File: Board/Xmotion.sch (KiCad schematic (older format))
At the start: 41 parts, among them J1 DB25, J2 DB25

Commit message: Board is layed out
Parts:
- added K1: FAN1, connect:SIL-3, symbol CONN_3
- added K4: FAN4, connect:SIL-3, symbol CONN_3
- added P100, P200, P300, P400: CONN_1, symbol CONN_1
- J1, J2: footprint (none) -> connect:DB25MC
- K2: renamed from K?; value FAN1 -> FAN2; footprint (none) -> connect:SIL-3
- K3: renamed from K?; value FAN2 -> FAN3; footprint (none) -> connect:SIL-3
- P1, P10, P11, P12, P13, P14, P15, P16, P17, P18, P19, P2, P20, P21, P22, P23, P24, P25, P3, P4, P5, P6, P7, P8, P9: renamed from P?; footprint (none) -> Xmotion:PLUGABLE_HEADER
- Q1, Q2, Q3, Q4, Q5, Q6: renamed from Q?; footprint TO220 -> Xmotion:TO220
- R1, R2, R3, R4, R5, R6: renamed from R?; footprint (none) -> discret:R3
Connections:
- wire segments 209 -> 213
- no-connect marks 7 -> 12

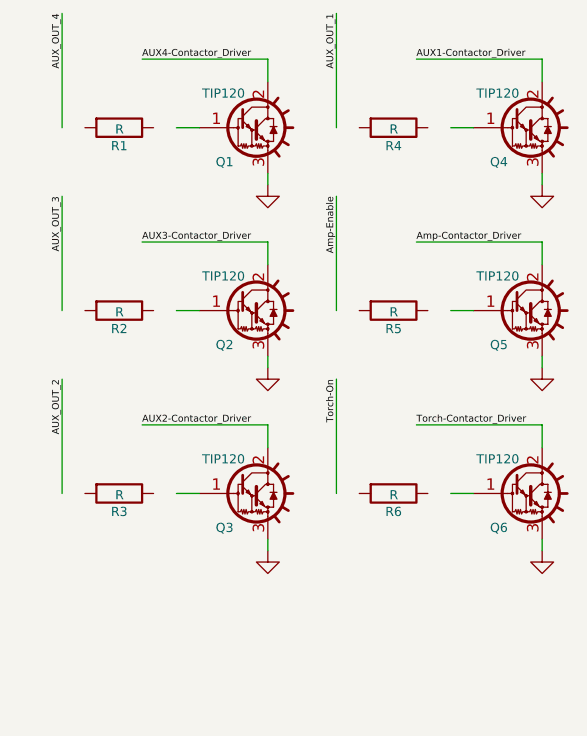
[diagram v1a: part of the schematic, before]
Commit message: Board is routed
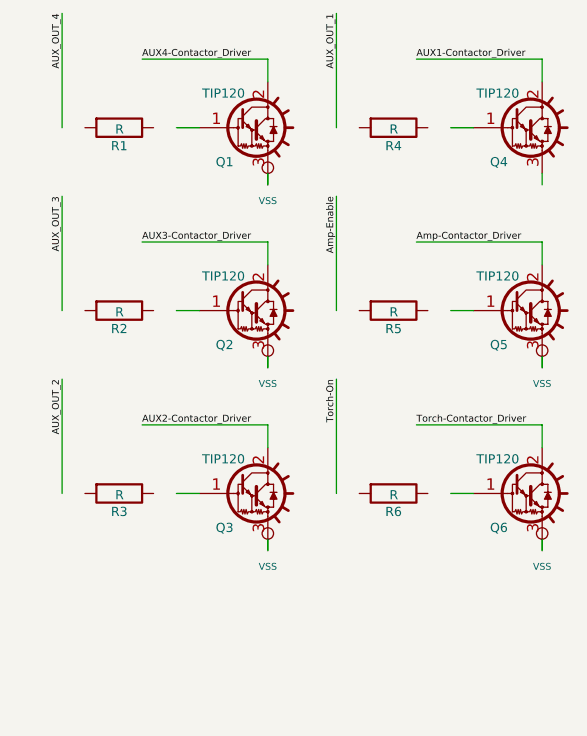
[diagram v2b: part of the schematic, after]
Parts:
- P100, P200, P300, P400: footprint (none) -> Xmotion:BOLT_HOLE
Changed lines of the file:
@@
-$EndComp
-$Comp
-L GND #PWR082
-U 1 1 59A7D273
-P 2300 5600
-F 0 "#PWR082" H 2300 5600 30  0001 C CNN
-F 1 "GND" H 2300 5530 30  0001 C CNN
-F 2 "" H 2300 5600 60  0001 C CNN
-F 3 "" H 2300 5600 60  0001 C CNN
-	1    2300 5600
-	-1   0    0    1
 $EndComp
 $Comp
@@
 	10800 5800 10800 5900
 $Comp
-L GND #PWR085
-U 1 1 59A7FBBE
-P 10800 6350
-F 0 "#PWR085" H 10800 6350 30  0001 C CNN
-F 1 "GND" H 10800 6280 30  0001 C CNN
-F 2 "" H 10800 6350 60  0001 C CNN
-F 3 "" H 10800 6350 60  0001 C CNN
-	1    10800 6350
-	1    0    0    -1
-$EndComp
-$Comp
 L R R6
 U 1 1 59A7FC06
@@
 	10800 5000 10800 5100
 $Comp
-L GND #PWR086
-U 1 1 59A80D25
-P 10800 5550
-F 0 "#PWR086" H 10800 5550 30  0001 C CNN
-F 1 "GND" H 10800 5480 30  0001 C CNN
-F 2 "" H 10800 5550 60  0001 C CNN
-F 3 "" H 10800 5550 60  0001 C CNN
-	1    10800 5550
-	1    0    0    -1
-$EndComp
-$Comp
 L R R5
 U 1 1 59A80D2B
@@
 Wire Wire Line
 	10800 4200 10800 4300
-$Comp
-L GND #PWR087
-U 1 1 59A81DC0
-P 10800 4750
-F 0 "#PWR087" H 10800 4750 30  0001 C CNN
-F 1 "GND" H 10800 4680 30  0001 C CNN
-F 2 "" H 10800 4750 60  0001 C CNN
-F 3 "" H 10800 4750 60  0001 C CNN
-	1    10800 4750
-	1    0    0    -1
-$EndComp
 $Comp
 L R R4
@@
 	9600 5800 9600 5900
 $Comp
-L GND #PWR088
-U 1 1 59A82CF5
-P 9600 6350
-F 0 "#PWR088" H 9600 6350 30  0001 C CNN
-F 1 "GND" H 9600 6280 30  0001 C CNN
-F 2 "" H 9600 6350 60  0001 C CNN
-F 3 "" H 9600 6350 60  0001 C CNN
-	1    9600 6350
-	1    0    0    -1
-$EndComp
-$Comp
 L R R3
 U 1 1 59A82CFB
@@
 	9600 5000 9600 5100
 $Comp
-L GND #PWR089
-U 1 1 59A83002
-P 9600 5550
-F 0 "#PWR089" H 9600 5550 30  0001 C CNN
-F 1 "GND" H 9600 5480 30  0001 C CNN
-F 2 "" H 9600 5550 60  0001 C CNN
-F 3 "" H 9600 5550 60  0001 C CNN
-	1    9600 5550
-	1    0    0    -1
-$EndComp
-$Comp
 L R R2
 U 1 1 59A83008
@@
 Wire Wire Line
 	9600 4200 9600 4300
-$Comp
-L GND #PWR090
-U 1 1 59A8377D
-P 9600 4750
-F 0 "#PWR090" H 9600 4750 30  0001 C CNN
-F 1 "GND" H 9600 4680 30  0001 C CNN
-F 2 "" H 9600 4750 60  0001 C CNN
-F 3 "" H 9600 4750 60  0001 C CNN
-	1    9600 4750
-	1    0    0    -1
-$EndComp
 $Comp
 L R R1
@@
 	1300 3900 1650 3900
 $Comp
-L GND #PWR091
+L GND #PWR085
 U 1 1 59A85377
 P 1650 4300
-F 0 "#PWR091" H 1650 4300 30  0001 C CNN
+F 0 "#PWR085" H 1650 4300 30  0001 C CNN
 F 1 "GND" H 1650 4230 30  0001 C CNN
 F 2 "" H 1650 4300 60  0001 C CNN
@@
 $EndComp
 $Comp
-L GND #PWR092
+L GND #PWR086
 U 1 1 59A8537D
 P 1650 4200
-F 0 "#PWR092" H 1650 4200 30  0001 C CNN
+F 0 "#PWR086" H 1650 4200 30  0001 C CNN
 F 1 "GND" H 1650 4130 30  0001 C CNN
 F 2 "" H 1650 4200 60  0001 C CNN
@@
 $EndComp
 $Comp
-L GND #PWR093
+L GND #PWR087
 U 1 1 59A85383
 P 1650 4100
-F 0 "#PWR093" H 1650 4100 30  0001 C CNN
+F 0 "#PWR087" H 1650 4100 30  0001 C CNN
 F 1 "GND" H 1650 4030 30  0001 C CNN
 F 2 "" H 1650 4100 60  0001 C CNN
@@
 $EndComp
 $Comp
-L GND #PWR094
+L GND #PWR088
 U 1 1 59A85389
 P 1650 4000
-F 0 "#PWR094" H 1650 4000 30  0001 C CNN
+F 0 "#PWR088" H 1650 4000 30  0001 C CNN
 F 1 "GND" H 1650 3930 30  0001 C CNN
 F 2 "" H 1650 4000 60  0001 C CNN
@@
 	1300 2800 1650 2800
 $Comp
-L GND #PWR095
+L GND #PWR089
 U 1 1 59A8538F
 P 1650 3900
-F 0 "#PWR095" H 1650 3900 30  0001 C CNN
+F 0 "#PWR089" H 1650 3900 30  0001 C CNN
 F 1 "GND" H 1650 3830 30  0001 C CNN
 F 2 "" H 1650 3900 60  0001 C CNN
@@
 $EndComp
 $Comp
-L VDD #PWR096
+L VDD #PWR090
 U 1 1 59A85CDF
 P 1650 3750
-F 0 "#PWR096" H 1650 3850 30  0001 C CNN
+F 0 "#PWR090" H 1650 3850 30  0001 C CNN
 F 1 "VDD" H 1650 3860 30  0000 C CNN
 F 2 "" H 1650 3750 60  0001 C CNN
@@
 $EndComp
 $Comp
-L VDD #PWR097
+L VDD #PWR091
 U 1 1 59A8618F
 P 1650 3650
-F 0 "#PWR097" H 1650 3750 30  0001 C CNN
+F 0 "#PWR091" H 1650 3750 30  0001 C CNN
 F 1 "VDD" H 1650 3760 30  0000 C CNN
 F 2 "" H 1650 3650 60  0001 C CNN
@@
 $EndComp
 $Comp
-L VDD #PWR098
+L VDD #PWR092
 U 1 1 59A8623E
 P 1650 3550
-F 0 "#PWR098" H 1650 3650 30  0001 C CNN
+F 0 "#PWR092" H 1650 3650 30  0001 C CNN
 F 1 "VDD" H 1650 3660 30  0000 C CNN
 F 2 "" H 1650 3550 60  0001 C CNN
@@
 $EndComp
 $Comp
-L VDD #PWR099
+L VDD #PWR093
 U 1 1 59A862C4
 P 1650 3450
-F 0 "#PWR099" H 1650 3550 30  0001 C CNN
+F 0 "#PWR093" H 1650 3550 30  0001 C CNN
 F 1 "VDD" H 1650 3560 30  0000 C CNN
 F 2 "" H 1650 3450 60  0001 C CNN
@@
 $EndComp
 $Comp
-L VDD #PWR0100
+L VDD #PWR094
 U 1 1 59A8634A
 P 1650 3350
-F 0 "#PWR0100" H 1650 3450 30  0001 C CNN
+F 0 "#PWR094" H 1650 3450 30  0001 C CNN
 F 1 "VDD" H 1650 3460 30  0000 C CNN
 F 2 "" H 1650 3350 60  0001 C CNN
@@
 $EndComp
 $Comp
-L +12V #PWR0101
+L +12V #PWR095
 U 1 1 59A865E5
 P 1650 3200
-F 0 "#PWR0101" H 1650 3150 20  0001 C CNN
+F 0 "#PWR095" H 1650 3150 20  0001 C CNN
 F 1 "+12V" H 1650 3300 30  0000 C CNN
 F 2 "" H 1650 3200 60  0001 C CNN
@@
 $EndComp
 $Comp
-L +12V #PWR0102
+L +12V #PWR096
 U 1 1 59A8694D
 P 1650 3100
-F 0 "#PWR0102" H 1650 3050 20  0001 C CNN
+F 0 "#PWR096" H 1650 3050 20  0001 C CNN
 F 1 "+12V" H 1650 3200 30  0000 C CNN
 F 2 "" H 1650 3100 60  0001 C CNN
@@
 $EndComp
 $Comp
-L +12V #PWR0103
+L +12V #PWR097
 U 1 1 59A869D3
 P 1650 3000
-F 0 "#PWR0103" H 1650 2950 20  0001 C CNN
+F 0 "#PWR097" H 1650 2950 20  0001 C CNN
 F 1 "+12V" H 1650 3100 30  0000 C CNN
 F 2 "" H 1650 3000 60  0001 C CNN
@@
 $EndComp
 $Comp
-L +12V #PWR0104
+L +12V #PWR098
 U 1 1 59A86A59
 P 1650 2900
-F 0 "#PWR0104" H 1650 2850 20  0001 C CNN
+F 0 "#PWR098" H 1650 2850 20  0001 C CNN
 F 1 "+12V" H 1650 3000 30  0000 C CNN
 F 2 "" H 1650 2900 60  0001 C CNN
@@
 $EndComp
 $Comp
-L +12V #PWR0105
+L +12V #PWR099
 U 1 1 59A86B08
 P 1650 2800
-F 0 "#PWR0105" H 1650 2750 20  0001 C CNN
+F 0 "#PWR099" H 1650 2750 20  0001 C CNN
 F 1 "+12V" H 1650 2900 30  0000 C CNN
 F 2 "" H 1650 2800 60  0001 C CNN
@@
 	9250 2650 9250 2400
 $Comp
-L GND #PWR0106
+L GND #PWR0100
 U 1 1 59A8789B
 P 9250 2400
-F 0 "#PWR0106" H 9250 2400 30  0001 C CNN
+F 0 "#PWR0100" H 9250 2400 30  0001 C CNN
 F 1 "GND" H 9250 2330 30  0001 C CNN
 F 2 "" H 9250 2400 60  0001 C CNN
@@
 $EndComp
 $Comp
-L +12V #PWR0107
+L +12V #PWR0101
 U 1 1 59A878A1
 P 9150 2400
-F 0 "#PWR0107" H 9150 2350 20  0001 C CNN
+F 0 "#PWR0101" H 9150 2350 20  0001 C CNN
 F 1 "+12V" H 9150 2500 30  0000 C CNN
 F 2 "" H 9150 2400 60  0001 C CNN
@@
 	10500 2650 10500 2400
 $Comp
-L GND #PWR0108
+L GND #PWR0102
 U 1 1 59A87976
 P 10500 2400
-F 0 "#PWR0108" H 10500 2400 30  0001 C CNN
+F 0 "#PWR0102" H 10500 2400 30  0001 C CNN
 F 1 "GND" H 10500 2330 30  0001 C CNN
 F 2 "" H 10500 2400 60  0001 C CNN
@@
 $EndComp
 $Comp
-L +12V #PWR0109
+L +12V #PWR0103
 U 1 1 59A8797C
 P 10400 2400
-F 0 "#PWR0109" H 10400 2350 20  0001 C CNN
+F 0 "#PWR0103" H 10400 2350 20  0001 C CNN
 F 1 "+12V" H 10400 2500 30  0000 C CNN
 F 2 "" H 10400 2400 60  0001 C CNN
@@
 F 0 "P100" H 3730 3250 40  0000 L CNN
 F 1 "CONN_1" H 3650 3305 30  0001 C CNN
-F 2 "" H 3650 3250 60  0000 C CNN
+F 2 "Xmotion:BOLT_HOLE" H 3650 3250 60  0001 C CNN
 F 3 "" H 3650 3250 60  0000 C CNN
 	1    3650 3250
@@
 F 0 "P200" H 3730 3400 40  0000 L CNN
 F 1 "CONN_1" H 3650 3455 30  0001 C CNN
-F 2 "" H 3650 3400 60  0000 C CNN
+F 2 "Xmotion:BOLT_HOLE" H 3650 3400 60  0001 C CNN
 F 3 "" H 3650 3400 60  0000 C CNN
 	1    3650 3400
@@
 F 0 "P300" H 3730 3550 40  0000 L CNN
 F 1 "CONN_1" H 3650 3605 30  0001 C CNN
-F 2 "" H 3650 3550 60  0000 C CNN
+F 2 "Xmotion:BOLT_HOLE" H 3650 3550 60  0001 C CNN
 F 3 "" H 3650 3550 60  0000 C CNN
 	1    3650 3550
@@
 F 0 "P400" H 3730 3700 40  0000 L CNN
 F 1 "CONN_1" H 3650 3755 30  0001 C CNN
-F 2 "" H 3650 3700 60  0000 C CNN
+F 2 "Xmotion:BOLT_HOLE" H 3650 3700 60  0001 C CNN
 F 3 "" H 3650 3700 60  0000 C CNN
 	1    3650 3700
@@
 NoConn ~ 3500 3550
 NoConn ~ 3500 3700
+$Comp
+L VSS #PWR0104
+U 1 1 59A90645
+P 9600 6350
+F 0 "#PWR0104" H 9600 6350 30  0001 C CNN
+F 1 "VSS" H 9600 6280 30  0000 C CNN
+F 2 "" H 9600 6350 60  0001 C CNN
+F 3 "" H 9600 6350 60  0001 C CNN
+	1    9600 6350
+	1    0    0    -1
+$EndComp
+$Comp
+L VSS #PWR0105
+U 1 1 59A90940
+P 10800 6350
+F 0 "#PWR0105" H 10800 6350 30  0001 C CNN
+F 1 "VSS" H 10800 6280 30  0000 C CNN
+F 2 "" H 10800 6350 60  0001 C CNN
+F 3 "" H 10800 6350 60  0001 C CNN
+	1    10800 6350
+	1    0    0    -1
+$EndComp
+$Comp
+L VSS #PWR0106
+U 1 1 59A90A65
+P 9600 5550
+F 0 "#PWR0106" H 9600 5550 30  0001 C CNN
+F 1 "VSS" H 9600 5480 30  0000 C CNN
+F 2 "" H 9600 5550 60  0001 C CNN
+F 3 "" H 9600 5550 60  0001 C CNN
+	1    9600 5550
+	1    0    0    -1
+$EndComp
+$Comp
+L VSS #PWR0107
+U 1 1 59A90AFD
+P 10800 5550
+F 0 "#PWR0107" H 10800 5550 30  0001 C CNN
+F 1 "VSS" H 10800 5480 30  0000 C CNN
+F 2 "" H 10800 5550 60  0001 C CNN
+F 3 "" H 10800 5550 60  0001 C CNN
+	1    10800 5550
+	1    0    0    -1
+$EndComp
+$Comp
+L VSS #PWR0108
+U 1 1 59A90BC4
+P 9600 4750
+F 0 "#PWR0108" H 9600 4750 30  0001 C CNN
+F 1 "VSS" H 9600 4680 30  0000 C CNN
+F 2 "" H 9600 4750 60  0001 C CNN
+F 3 "" H 9600 4750 60  0001 C CNN
+	1    9600 4750
+	1    0    0    -1
+$EndComp
+$Comp
+L GND #PWR082
+U 1 1 59A7D273
+P 2300 5600
+F 0 "#PWR082" H 2300 5600 30  0001 C CNN
+F 1 "GND" H 2300 5530 30  0001 C CNN
+F 2 "" H 2300 5600 60  0001 C CNN
+F 3 "" H 2300 5600 60  0001 C CNN
+	1    2300 5600
+	-1   0    0    1
+$EndComp
 $EndSCHEMATC

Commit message: Updated Schematic, fixed pinmap to work with Mesa 5i25 G540 Firmware and added opto-isolators
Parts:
- removed P100, P200, P300, P400: CONN_1, Xmotion:BOLT_HOLE, symbol CONN_1
- removed Q2, Q3, Q4, Q5, Q6: TIP120, Xmotion:TO220, symbol TIP120
- removed R2, R3, R4, R5, R6: R, discret:R3, symbol R
- added Q? (x5): TIP120, Xmotion:TO220, symbol TIP120
- added R? (x6): 220, symbol R
- added R? (x5): 1K, discret:R3, symbol R
- added U? (x6): 4N25, DIP-6, symbol 4N25
- K1, K2, K3, K4: symbol CONN_3 -> CONN_01X03
- P1, P10, P11, P12, P13, P14, P15, P16, P17, P18, P19, P2, P20, P21, P22, P23, P24, P25, P3, P4, P5, P6, P7, P8, P9: symbol CONN_5 -> CONN_01X05
- R1: value R -> 1K
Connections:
- net labels added: Y1-Home, Y2-Home
- wire segments 213 -> 261
- no-connect marks 12 -> 13
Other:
- moved on the sheet: K1, K2, K3, K4, Q1, R1

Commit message: Board is ready to be routed
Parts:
- J1, J2: footprint connect:DB25MC -> Xmotion:DB25MC
- U1, U2, U3, U4, U5, U6: renamed from U?; footprint DIP-6 -> Housings_DIP:DIP-6_W7.62mm
- gave numbers to parts that had none: 16
- renumbered R1 to R7
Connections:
- net Y-Home is gone; now on net Y1-Home: P15.2 (P2)
- net GND: no longer P10.1 (P1), P14.1 (P1), P19.1 (P1), P6.1 (P1), R1.2, R2.2, R3.2, R4.2, R5.2, R6.2
- net VSS: now also P10.1 (P1), P14.1 (P1), P19.1 (P1), P6.1 (P1), R1.2, R2.2, R3.2, R4.2, R5.2, R6.2; no longer P15.4 (P4)
- net Y2-Home: now also P15.3 (P3)
- net Z-Home: now also P15.4 (P4); no longer P15.3 (P3)

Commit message: Ready to fabricate second revision
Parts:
- added HOLE1, HOLE2: Conn_01x01, Xmotion:BOLT_HOLE, symbol Conn_01x01
- K1, K2, K3, K4: footprint connect:SIL-3 -> Xmotion:SIL-3
- R1, R2, R3, R4, R5, R6: footprint (none) -> Xmotion:R3
- R10, R11, R12, R7, R8, R9: footprint discret:R3 -> Xmotion:R3
- U1, U2, U3, U4, U5, U6: footprint Housings_DIP:DIP-6_W7.62mm -> Xmotion:DIP-6
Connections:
- net GND: now also HOLE1.1 (Pin_1), HOLE2.1 (Pin_1)
- net VSS: no longer P7.5 (P5)
- net Z-Touch: now also P7.5 (P5)
